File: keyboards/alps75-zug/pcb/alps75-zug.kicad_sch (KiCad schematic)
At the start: 176 parts, among them SW1 SW_Push, SW10 SW_Push, SW11 SW_Push, SW12 SW_Push, SW13 SW_Push, SW14 SW_Push, SW15 SW_Push, SW16 SW_Push, SW17 SW_Push, SW18 SW_Push, SW19 SW_Push, SW2 SW_Push, SW20 SW_Push, SW21 SW_Push, SW22 SW_Push, SW23 SW_Push, SW24 SW_Push, SW25 SW_Push, SW26 SW_Push, SW27 SW_Push, SW28 SW_Push, SW29 SW_Push, SW3 SW_Push, SW30 SW_Push, SW31 SW_Push, SW32 SW_Push, SW33 SW_Push, SW34 SW_Push, SW35 SW_Push, SW36 SW_Push, SW37 SW_Push, SW38 SW_Push, SW39 SW_Push, SW4 SW_Push, SW40 SW_Push, SW41 SW_Push, SW42 SW_Push, SW43 SW_Push, SW44 SW_Push, SW45 SW_Push, SW46 SW_Push, SW47 SW_Push, SW48 SW_Push, SW49 SW_Push, SW5 SW_Push, SW50 SW_Push, SW51 SW_Push, SW52 SW_Push, SW53 SW_Push, SW54 SW_Push, SW55 SW_Push, SW56 SW_Push, SW57 SW_Push, SW58 SW_Push, SW59 SW_Push, SW6 SW_Push, SW60 SW_Push, SW61 SW_Push, SW62 SW_Push, SW63 SW_Push, SW64 SW_Push, SW65 SW_Push, SW66 SW_Push, SW67 SW_Push, SW68 SW_Push, SW69 SW_Push, SW7 SW_Push, SW70 SW_Push, SW71 SW_Push, SW72 SW_Push, SW73 SW_Push, SW74 SW_Push, SW75 SW_Push, SW76 SW_Push, SW77 SW_Push, SW78 SW_Push, SW79 SW_Push, SW8 SW_Push, SW80 SW_Push, SW81 SW_Push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

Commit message: Derive the alps75-zug board outline, mounting holes and stab slots from the plate
The board had no Edge.Cuts geometry and no mounting holes at all. All of
this now comes from alps75-zug-keyboard-plate.jscad, with y negated since
the plate is authored y-up and KiCad is y-down:

- Edge.Cuts is the plate outline: 340.3 x 130.735 mm, 4 mm corner radius,
  x -17.75..322.55, y -16.4005..114.3345.
- H1..H8 are MountingHole_3.2mm_M3 at the plate's eight drill positions
  (y 12.4 top / -110.335 bottom in plate coords). The exported Excellon
  matches the plate hole set exactly, tool T2C3.200, no extras, none
  missing.
- The twelve Alps AEK stabiliser slots are reproduced on Dwgs.User as
  documentation outlines only. AEK stabs are plate-mount -- the insert
  clips into the plate and the wire runs in the plate-to-PCB gap -- and
  ai03's Alps_Solderable footprints put no stab holes on the PCB either,
  so cutting them here would only cost routing area.

H1..H8 are in the schematic too, so the next "Update PCB from Schematic"
does not delete the footprints.

DRC 0 violations, ERC 0 violations, schematic parity clean for everything
added (the 88 remaining parity warnings are the pre-existing Sim.Device
field mismatch on the kbplacer-generated diodes).

Co-Authored-By: Claude Opus 5 <noreply@anthropic.com>
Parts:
- added H1, H2, H3, H4, H5, H6, H7, H8: MountingHole_3.2mm_M3, MountingHole:MountingHole_3.2mm_M3, symbol Mechanical:MountingHole
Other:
- note added: "Plate mounting holes - 8 x 3.2 mm NPTH for M3, positions and diameter taken from alps75-zug-keyboard-plate.jscad"

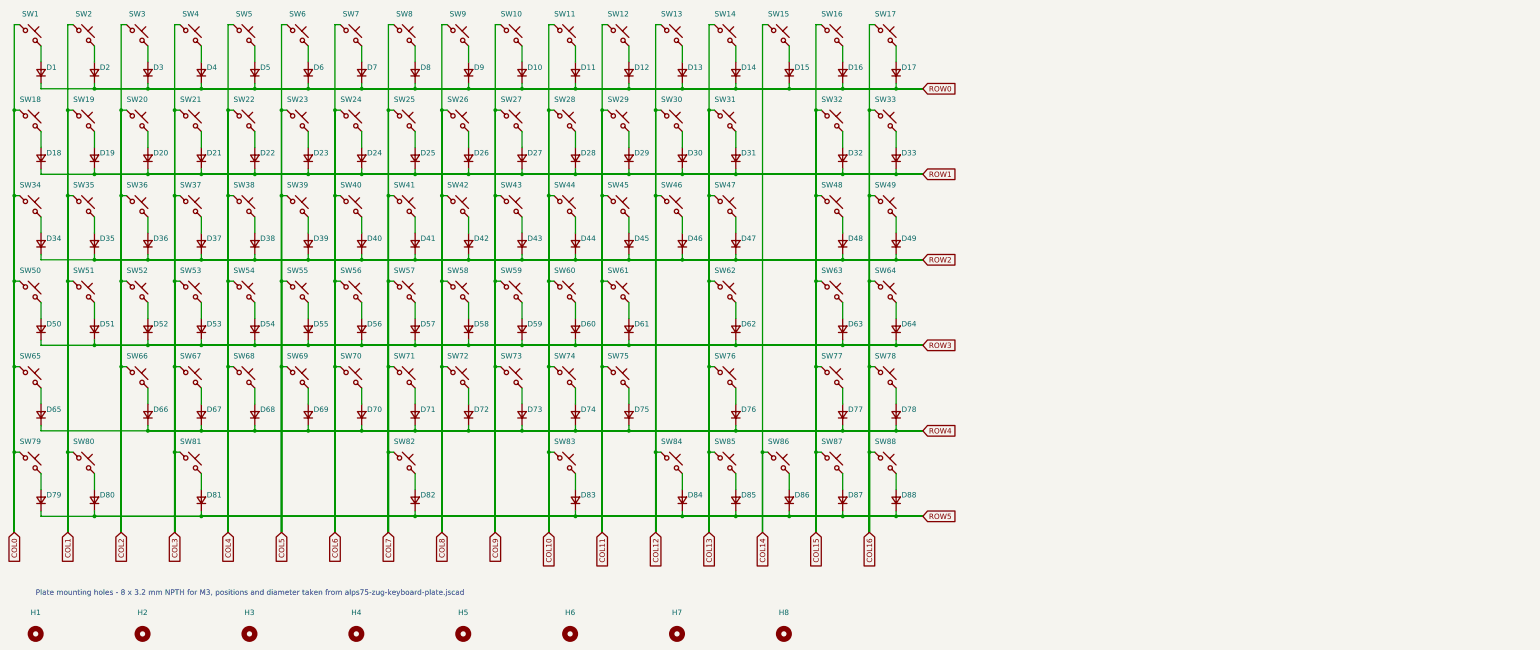
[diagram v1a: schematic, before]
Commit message: Add RP2040 (U1) to alps75-zug and wire the key matrix to it
Schematic: add an RP2040 (QFN-56 7x7mm) with the 6 ROW and 17 COL
global labels attached to its GPIOs, so every matrix net now ends on
U1. Power, USB, QSPI flash, crystal, SWD and RUN pins are still
unconnected. The 8 Mechanical:MountingHole symbols are removed.

PCB, after update from schematic:
- U1 placed on F.Cu at (296.275, 227.6), below the key area, with the
  ROW/COL fan-out routed (129 new segments, 6 vias on the ROW nets).
- Mounting holes H1-H8 removed, following the schematic.
- Rounded Edge.Cuts outline replaced by a 358 x 172.5 mm rectangle
  enlarged to take the controller area.
- Footprints and existing tracks moved by (-8.5, +51.3) mm.

Also picks up the local KiCad view state (.kicad_prl) and U1 in the
used designators (.kicad_pro).

Co-Authored-By: Claude Opus 5 <noreply@anthropic.com>
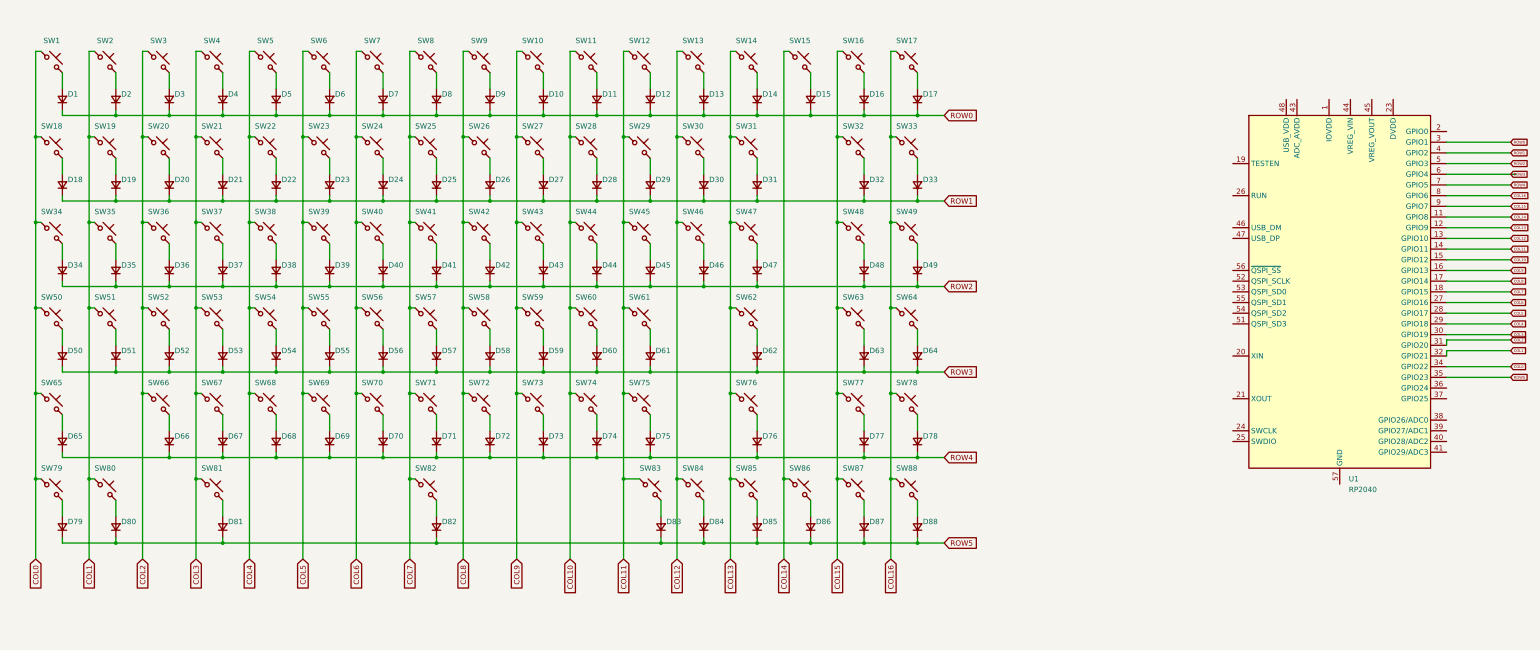
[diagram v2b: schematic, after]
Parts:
- removed H1, H2, H3, H4, H5, H6, H7, H8: MountingHole_3.2mm_M3, MountingHole:MountingHole_3.2mm_M3, symbol Mechanical:MountingHole
- added U1: RP2040, Package_DFN_QFN:QFN-56-1EP_7x7mm_P0.4mm_EP3.2x3.2mm, symbol MCU_RaspberryPi:RP2040
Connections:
- net COL0: now also U1.34 (GPIO22)
- net COL1: now also U1.32 (GPIO21)
- net COL10: now also U1.15 (GPIO12); no longer SW83.1
- net COL11: now also SW83.1, U1.14 (GPIO11)
- net COL12: now also U1.13 (GPIO10)
- net COL13: now also U1.12 (GPIO9)
- net COL14: now also U1.11 (GPIO8)
- net COL15: now also U1.9 (GPIO7)
- net COL16: now also U1.8 (GPIO6)
- net COL2: now also U1.31 (GPIO20)
- net COL3: now also U1.30 (GPIO19)
- net COL4: now also U1.29 (GPIO18)
- net COL5: now also U1.28 (GPIO17)
- net COL6: now also U1.27 (GPIO16)
- net COL7: now also U1.18 (GPIO15)
- net COL8: now also U1.17 (GPIO14)
- net COL9: now also U1.16 (GPIO13)
- net ROW0: now also U1.3 (GPIO1)
- net ROW1: now also U1.4 (GPIO2)
- net ROW2: now also U1.5 (GPIO3)
- net ROW3: now also U1.6 (GPIO4)
- net ROW4: now also U1.7 (GPIO5)
- net ROW5: now also U1.35 (GPIO23)
- new net: U1.1 (IOVDD), U1.10 (IOVDD), U1.22 (IOVDD), U1.33 (IOVDD), U1.42 (IOVDD), U1.49 (IOVDD)
- new net: U1.23 (DVDD), U1.50 (DVDD)
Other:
- note removed: "Plate mounting holes - 8 x 3.2 mm NPTH for M3, positions and diameter taken from alps75-zug-keyboard-plate.jscad"
- moved on the sheet: D1, D10, D11, D12, D13, D14, D15, D16, D17, D18, D19, D2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
